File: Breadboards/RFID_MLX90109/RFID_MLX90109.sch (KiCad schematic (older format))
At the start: 0 parts

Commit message: Transfers RFID schematic from Nestbox_v2 into BB
The RFID part of the Nestbox_v2 schematic was spun out into the MLX90109
BB schematic.
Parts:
- added AE?: Antenna_Loop, symbol Antenna_Loop
- added AE? (x6): Antenna_Dipole, symbol Antenna_Dipole
- added C? (x5): C, symbol C
- added JP?: Jumper_SELECT_Dual, symbol Jumper_SELECT_Dual
- added Q?: Q_NMOS_DGS, symbol Q_NMOS_DGS
- added R?: 36k, symbol R
- added R?: 100k, symbol R
- added R? (x6): R, symbol R
- added U?: MLX90109, symbol MLX90109
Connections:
- new net: AE?.1, AE?.1, AE?.1, C?.2, C?.2, C?.2, C?.2, U?.1 (COIL)
- new net: R?.1, R?.1, U?.3 (SPEED)
- new net: C?.1, R?.1, R?.2, U?.4 (MODU)
- new net: R?.1, R?.2, U?.5 (MODE)
- new net: Q?.1 (D), R?.1
- new net: AE?.1, AE?.2 (x4)
- new net +3V3: JP?.3
- new net +5V: JP?.1
- new net GND: Q?.3 (S), R?.1, R?.2, U?.2 (VSS)
- new net RFID_CLOCK: R?.2, U?.6 (CLOCK)
- new net RFID_DATA: R?.2, U?.7 (DATA)
- new net RFID_MODU_N: Q?.2 (G)
- new net RFID_VDD: AE?.2, AE?.2, AE?.2, C?.1, C?.1, C?.1, C?.1, C?.2, JP?.2, R?.1, R?.1, R?.2, R?.2, R?.2, U?.8 (VDD)
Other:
- note added: "0.87 V"
- note added: "Pull to GND for Operation\nPull to VDD for Standby\n"

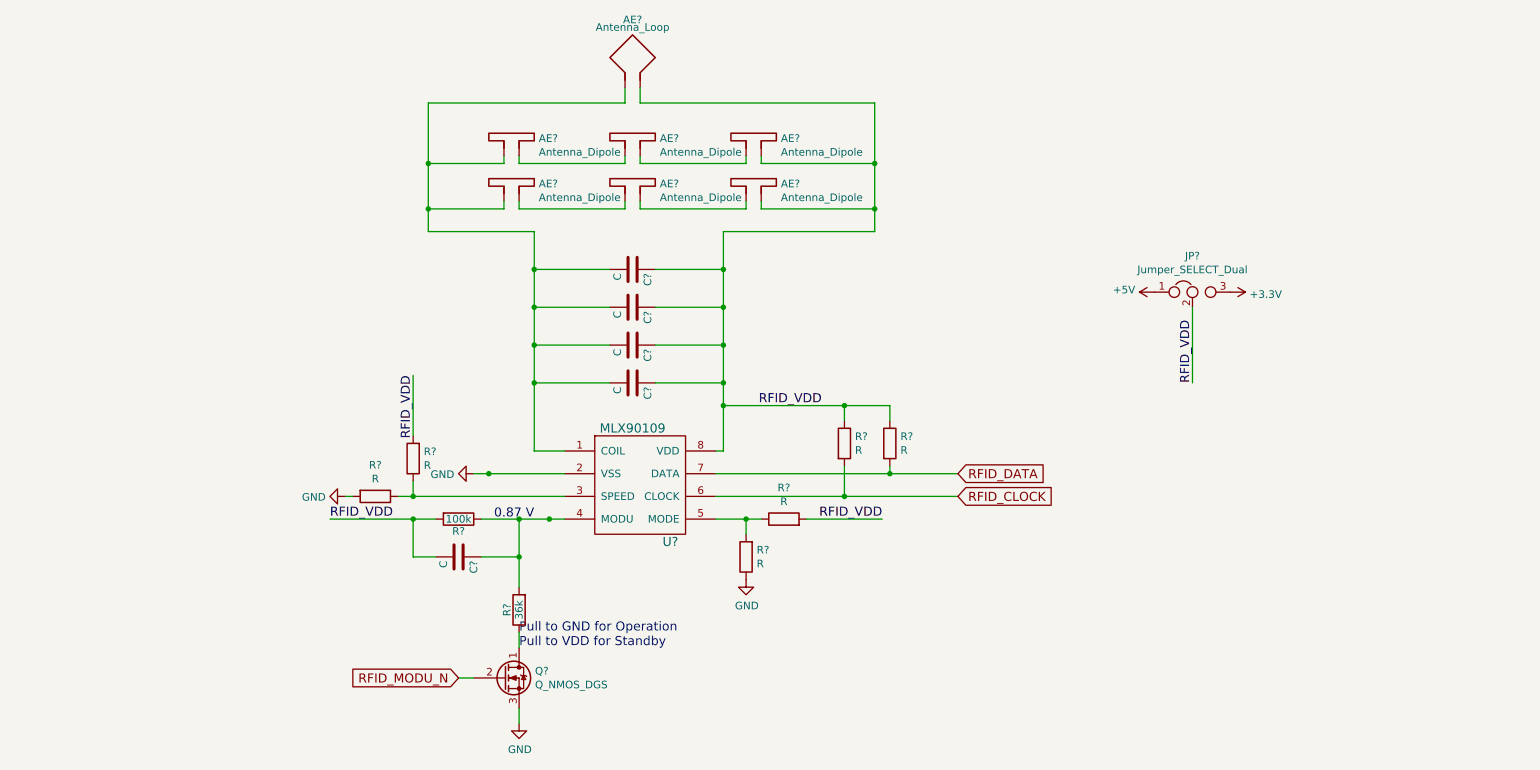
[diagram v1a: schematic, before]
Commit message: Adds connector for all signals
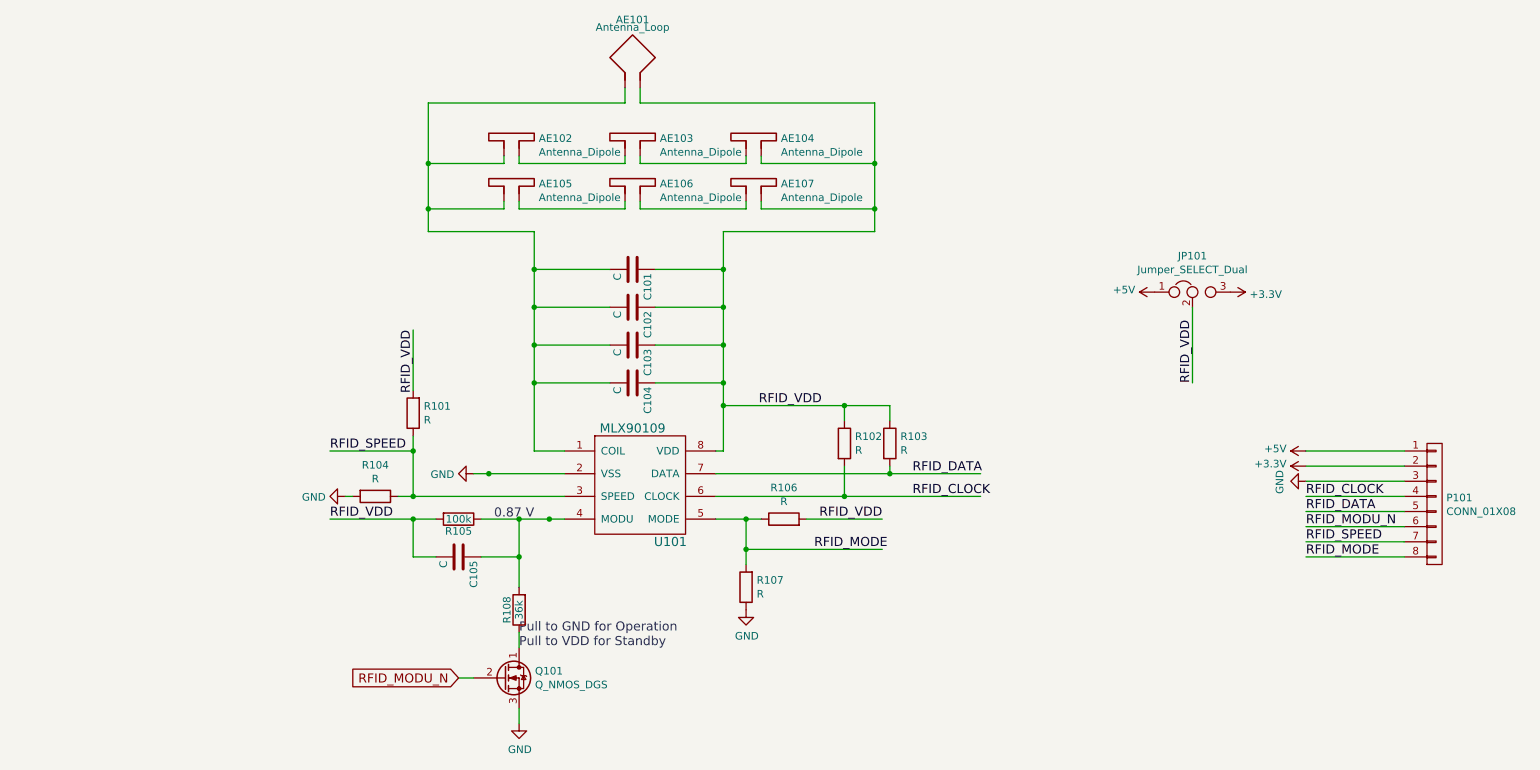
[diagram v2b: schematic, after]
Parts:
- added P101: CONN_01X08, symbol CONN_01X08
- gave numbers to parts that had none: 23
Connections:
- net labels added: RFID_MODE, RFID_SPEED
- wire segments 65 -> 75
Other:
- moved on the sheet: R101, R107

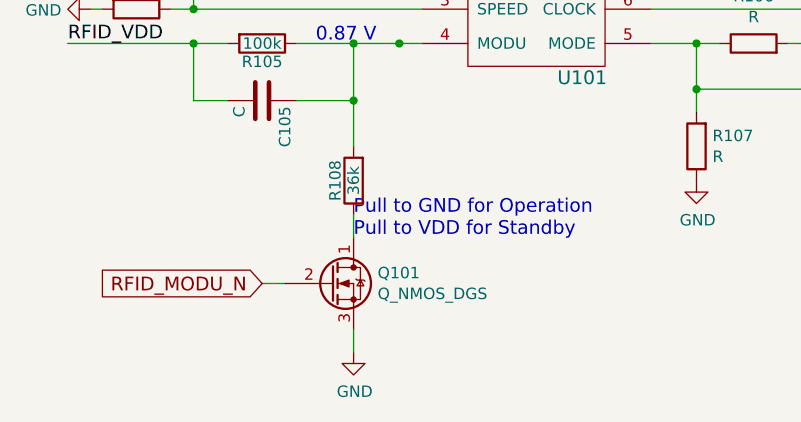
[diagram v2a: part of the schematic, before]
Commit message: Maps all components to Footprints
- All components have a now a footprint associated.
- The Pull down MOSFET was changed to GSD, to follow the SOT-23 package.
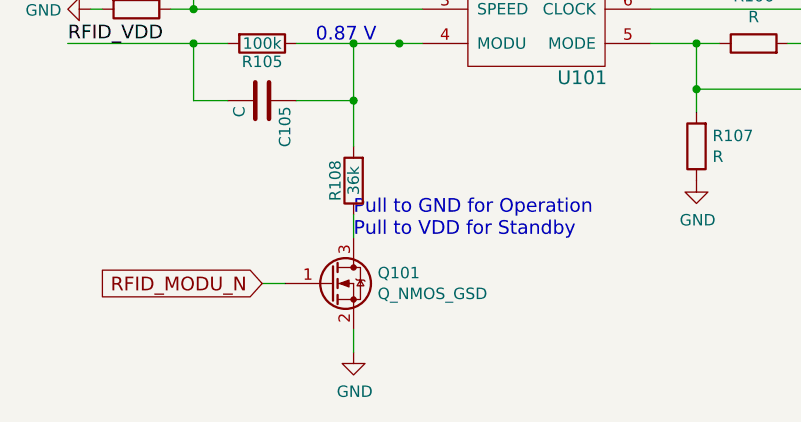
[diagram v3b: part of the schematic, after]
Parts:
- removed Q101: Q_NMOS_DGS, symbol Q_NMOS_DGS
- added Q101: Q_NMOS_GSD, TO_SOT_Packages_SMD:SOT-23_Handsoldering, symbol Q_NMOS_GSD
- AE101: footprint (none) -> Resistors_THT:R_Axial_DIN0411_L9.9mm_D3.6mm_P25.40mm_Horizontal
- AE102, AE103, AE104, AE105, AE106, AE107: footprint (none) -> Octanis3:TDK_B82450A
- C101, C102: footprint (none) -> Capacitors_THT:C_Rect_L7.0mm_W3.5mm_P5.00mm
- C103, C104, C105: footprint (none) -> Capacitors_SMD:C_0805_HandSoldering
- JP101: footprint (none) -> Pin_Headers:Pin_Header_Straight_1x03_Pitch2.54mm
- P101: footprint (none) -> Pin_Headers:Pin_Header_Straight_1x08_Pitch2.54mm
- R101, R102, R103, R104, R105, R106, R107, R108: footprint (none) -> Resistors_SMD:R_0603_HandSoldering
- U101: footprint (none) -> Housings_SOIC:SOIC-8_3.9x4.9mm_Pitch1.27mm
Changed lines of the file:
@@
 F 0 "U101" H 5500 2600 60  0000 C CNN
 F 1 "MLX90109" H 5250 3350 60  0000 C CNN
-F 2 "" H 5250 3350 60  0001 C CNN
+F 2 "Housings_SOIC:SOIC-8_3.9x4.9mm_Pitch1.27mm" H 5250 3350 60  0001 C CNN
 F 3 "" H 5250 3350 60  0001 C CNN
 	1    5250 3350
@@
 F 0 "R108" V 4580 4550 50  0000 C CNN
 F 1 "36k" V 4500 4550 50  0000 C CNN
-F 2 "" V 4430 4550 50  0001 C CNN
+F 2 "Resistors_SMD:R_0603_HandSoldering" V 4430 4550 50  0001 C CNN
 F 3 "" H 4500 4550 50  0001 C CNN
 	1    4500 4550
@@
 F 0 "R105" V 4180 3950 50  0000 C CNN
 F 1 "100k" V 4100 3950 50  0000 C CNN
-F 2 "" V 4030 3950 50  0001 C CNN
+F 2 "Resistors_SMD:R_0603_HandSoldering" V 4030 3950 50  0001 C CNN
 F 3 "" H 4100 3950 50  0001 C CNN
 	1    4100 3950
@@
 F 0 "C104" H 5275 3150 50  0000 L CNN
 F 1 "C" H 5275 2950 50  0000 L CNN
-F 2 "" H 5288 2900 50  0001 C CNN
+F 2 "Capacitors_SMD:C_0805_HandSoldering" H 5288 2900 50  0001 C CNN
 F 3 "" H 5250 3050 50  0001 C CNN
 	1    5250 3050
@@
 F 0 "AE101" H 5250 1150 50  0000 C CNN
 F 1 "Antenna_Loop" H 5250 1100 50  0000 C CNN
-F 2 "" H 5200 900 50  0001 C CNN
+F 2 "Resistors_THT:R_Axial_DIN0411_L9.9mm_D3.6mm_P25.40mm_Horizontal" H 5200 900 50  0001 C CNN
 F 3 "" H 5200 900 50  0001 C CNN
 	1    5200 900
@@
 F 0 "C105" H 4125 4300 50  0000 L CNN
 F 1 "C" H 4125 4100 50  0000 L CNN
-F 2 "" H 4138 4050 50  0001 C CNN
+F 2 "Capacitors_SMD:C_0805_HandSoldering" H 4138 4050 50  0001 C CNN
 F 3 "" H 4100 4200 50  0001 C CNN
 	1    4100 4200
@@
 F 0 "C103" H 5275 2900 50  0000 L CNN
 F 1 "C" H 5275 2700 50  0000 L CNN
-F 2 "" H 5288 2650 50  0001 C CNN
+F 2 "Capacitors_SMD:C_0805_HandSoldering" H 5288 2650 50  0001 C CNN
 F 3 "" H 5250 2800 50  0001 C CNN
 	1    5250 2800
@@
 F 0 "C102" H 5275 2650 50  0000 L CNN
 F 1 "C" H 5275 2450 50  0000 L CNN
-F 2 "" H 5288 2400 50  0001 C CNN
+F 2 "Capacitors_THT:C_Rect_L7.0mm_W3.5mm_P5.00mm" H 5288 2400 50  0001 C CNN
 F 3 "" H 5250 2550 50  0001 C CNN
 	1    5250 2550
@@
 F 0 "C101" H 5275 2400 50  0000 L CNN
 F 1 "C" H 5275 2200 50  0000 L CNN
-F 2 "" H 5288 2150 50  0001 C CNN
+F 2 "Capacitors_THT:C_Rect_L7.0mm_W3.5mm_P5.00mm" H 5288 2150 50  0001 C CNN
 F 3 "" H 5250 2300 50  0001 C CNN
 	1    5250 2300
@@
 $EndComp
 $Comp
-L +3.3V #PWR102
+L +3.3V #PWR01
 U 1 1 5A0F0963
 P 9200 2450
-F 0 "#PWR102" H 9200 2300 50  0001 C CNN
+F 0 "#PWR01" H 9200 2300 50  0001 C CNN
 F 1 "+3.3V" V 9215 2578 50  0000 L CNN
 F 2 "" H 9200 2450 50  0000 C CNN
@@
 F 0 "JP101" H 8950 2689 50  0000 C CNN
 F 1 "Jumper_SELECT_Dual" H 8950 2598 50  0000 C CNN
-F 2 "" H 8950 2450 50  0001 C CNN
+F 2 "Pin_Headers:Pin_Header_Straight_1x03_Pitch2.54mm" H 8950 2450 50  0001 C CNN
 F 3 "" H 8950 2450 50  0001 C CNN
 	1    8950 2450
@@
 RFID_VDD
 $Comp
-L +5V #PWR101
+L +5V #PWR02
 U 1 1 5A0F0965
 P 8700 2450
-F 0 "#PWR101" H 8700 2300 50  0001 C CNN
+F 0 "#PWR02" H 8700 2300 50  0001 C CNN
 F 1 "+5V" V 8715 2578 50  0000 L CNN
 F 2 "" H 8700 2450 50  0001 C CNN
@@
 $EndComp
 $Comp
-L GND #PWR105
+L GND #PWR03
 U 1 1 5A0F0966
 P 4200 3650
-F 0 "#PWR105" H 4200 3400 50  0001 C CNN
+F 0 "#PWR03" H 4200 3400 50  0001 C CNN
 F 1 "GND" V 4205 3522 50  0000 R CNN
 F 2 "" H 4200 3650 50  0001 C CNN
@@
 F 0 "R104" V 3343 3800 50  0000 C CNN
 F 1 "R" V 3434 3800 50  0000 C CNN
-F 2 "" V 3480 3800 50  0001 C CNN
+F 2 "Resistors_SMD:R_0603_HandSoldering" V 3480 3800 50  0001 C CNN
 F 3 "" H 3550 3800 50  0001 C CNN
 	1    3550 3800
@@
 F 0 "R101" H 3730 3204 50  0000 R CNN
 F 1 "R" H 3730 3295 50  0000 R CNN
-F 2 "" V 3730 3250 50  0001 C CNN
+F 2 "Resistors_SMD:R_0603_HandSoldering" V 3730 3250 50  0001 C CNN
 F 3 "" H 3800 3250 50  0001 C CNN
 	1    3800 3250
@@
 RFID_VDD
 $Comp
-L GND #PWR107
+L GND #PWR04
 U 1 1 5A0F0969
 P 3350 3800
-F 0 "#PWR107" H 3350 3550 50  0001 C CNN
+F 0 "#PWR04" H 3350 3550 50  0001 C CNN
 F 1 "GND" V 3355 3672 50  0000 R CNN
 F 2 "" H 3350 3800 50  0001 C CNN
@@
 F 0 "R107" H 5930 4354 50  0000 R CNN
 F 1 "R" H 5930 4445 50  0000 R CNN
-F 2 "" V 5930 4400 50  0001 C CNN
+F 2 "Resistors_SMD:R_0603_HandSoldering" V 5930 4400 50  0001 C CNN
 F 3 "" H 6000 4400 50  0001 C CNN
 	1    6000 4400
@@
 F 0 "R106" V 6457 3950 50  0000 C CNN
 F 1 "R" V 6366 3950 50  0000 C CNN
-F 2 "" V 6180 3950 50  0001 C CNN
+F 2 "Resistors_SMD:R_0603_HandSoldering" V 6180 3950 50  0001 C CNN
 F 3 "" H 6250 3950 50  0001 C CNN
 	1    6250 3950
@@
 $EndComp
 $Comp
-L GND #PWR108
+L GND #PWR05
 U 1 1 5A0F096C
 P 6000 4550
-F 0 "#PWR108" H 6000 4300 50  0001 C CNN
+F 0 "#PWR05" H 6000 4300 50  0001 C CNN
 F 1 "GND" H 6005 4377 50  0000 C CNN
 F 2 "" H 6000 4550 50  0001 C CNN
@@
 RFID_VDD
 $Comp
-L Q_NMOS_DGS Q101
-U 1 1 5A0F096D
-P 4400 5000
-F 0 "Q101" H 4605 5046 50  0000 L CNN
-F 1 "Q_NMOS_DGS" H 4605 4955 50  0000 L CNN
-F 2 "" H 4600 5100 50  0001 C CNN
-F 3 "" H 4400 5000 50  0001 C CNN
-	1    4400 5000
-	1    0    0    -1
-$EndComp
-$Comp
-L GND #PWR109
+L GND #PWR06
 U 1 1 5A0F096E
 P 4500 5300
-F 0 "#PWR109" H 4500 5050 50  0001 C CNN
+F 0 "#PWR06" H 4500 5050 50  0001 C CNN
 F 1 "GND" H 4505 5127 50  0000 C CNN
 F 2 "" H 4500 5300 50  0001 C CNN
@@
 F 0 "R102" H 6720 3496 50  0000 L CNN
 F 1 "R" H 6720 3405 50  0000 L CNN
-F 2 "" V 6580 3450 50  0001 C CNN
+F 2 "Resistors_SMD:R_0603_HandSoldering" V 6580 3450 50  0001 C CNN
 F 3 "" H 6650 3450 50  0001 C CNN
 	1    6650 3450
@@
 F 0 "R103" H 7020 3496 50  0000 L CNN
 F 1 "R" H 7020 3405 50  0000 L CNN
-F 2 "" V 6880 3450 50  0001 C CNN
+F 2 "Resistors_SMD:R_0603_HandSoldering" V 6880 3450 50  0001 C CNN
 F 3 "" H 6950 3450 50  0001 C CNN
 	1    6950 3450
@@
 F 0 "AE102" H 4630 1266 50  0000 L CNN
 F 1 "Antenna_Dipole" H 4630 1175 50  0000 L CNN
-F 2 "" H 4400 1350 50  0001 C CNN
+F 2 "Octanis3:TDK_B82450A" H 4400 1350 50  0001 C CNN
 F 3 "" H 4400 1350 50  0001 C CNN
 	1    4400 1350
@@
 F 0 "AE103" H 5430 1266 50  0000 L CNN
 F 1 "Antenna_Dipole" H 5430 1175 50  0000 L CNN
-F 2 "" H 5200 1350 50  0001 C CNN
+F 2 "Octanis3:TDK_B82450A" H 5200 1350 50  0001 C CNN
 F 3 "" H 5200 1350 50  0001 C CNN
 	1    5200 1350
@@
 F 0 "AE104" H 6230 1266 50  0000 L CNN
 F 1 "Antenna_Dipole" H 6230 1175 50  0000 L CNN
-F 2 "" H 6000 1350 50  0001 C CNN
+F 2 "Octanis3:TDK_B82450A" H 6000 1350 50  0001 C CNN
 F 3 "" H 6000 1350 50  0001 C CNN
 	1    6000 1350
@@
 F 0 "AE105" H 4630 1566 50  0000 L CNN
 F 1 "Antenna_Dipole" H 4630 1475 50  0000 L CNN
-F 2 "" H 4400 1650 50  0001 C CNN
+F 2 "Octanis3:TDK_B82450A" H 4400 1650 50  0001 C CNN
 F 3 "" H 4400 1650 50  0001 C CNN
 	1    4400 1650
@@
 F 0 "AE106" H 5430 1566 50  0000 L CNN
 F 1 "Antenna_Dipole" H 5430 1475 50  0000 L CNN
-F 2 "" H 5200 1650 50  0001 C CNN
+F 2 "Octanis3:TDK_B82450A" H 5200 1650 50  0001 C CNN
 F 3 "" H 5200 1650 50  0001 C CNN
 	1    5200 1650
@@
 F 0 "AE107" H 6230 1566 50  0000 L CNN
 F 1 "Antenna_Dipole" H 6230 1475 50  0000 L CNN
-F 2 "" H 6000 1650 50  0001 C CNN
+F 2 "Octanis3:TDK_B82450A" H 6000 1650 50  0001 C CNN
 F 3 "" H 6000 1650 50  0001 C CNN
 	1    6000 1650
@@
 RFID_MODU_N
 $Comp
-L +5V #PWR103
+L +5V #PWR07
 U 1 1 5A12CC37
 P 9700 3500
-F 0 "#PWR103" H 9700 3350 50  0001 C CNN
+F 0 "#PWR07" H 9700 3350 50  0001 C CNN
 F 1 "+5V" V 9715 3628 50  0000 L CNN
 F 2 "" H 9700 3500 50  0001 C CNN
@@
 $EndComp
 $Comp
-L +3.3V #PWR104
+L +3.3V #PWR08
 U 1 1 5A12CC72
 P 9700 3600
-F 0 "#PWR104" H 9700 3450 50  0001 C CNN
+F 0 "#PWR08" H 9700 3450 50  0001 C CNN
 F 1 "+3.3V" V 9715 3728 50  0000 L CNN
 F 2 "" H 9700 3600 50  0000 C CNN
@@
 $EndComp
 $Comp
-L GND #PWR106
+L GND #PWR09
 U 1 1 5A12CCDD
 P 9700 3700
-F 0 "#PWR106" H 9700 3450 50  0001 C CNN
+F 0 "#PWR09" H 9700 3450 50  0001 C CNN
 F 1 "GND" H 9705 3527 50  0000 C CNN
 F 2 "" H 9700 3700 50  0001 C CNN
@@
 F 0 "P101" H 10628 3891 50  0000 L CNN
 F 1 "CONN_01X08" H 10628 3800 50  0000 L CNN
-F 2 "" H 10550 3850 50  0000 C CNN
+F 2 "Pin_Headers:Pin_Header_Straight_1x08_Pitch2.54mm" H 10550 3850 50  0001 C CNN
 F 3 "" H 10550 3850 50  0000 C CNN
 	1    10550 3850
@@
 Text Label 9700 4200 0    60   ~ 0
 RFID_MODE
+$Comp
+L Q_NMOS_GSD Q101
+U 1 1 5A12C975
+P 4400 5000
+F 0 "Q101" H 4605 5046 50  0000 L CNN
+F 1 "Q_NMOS_GSD" H 4605 4955 50  0000 L CNN
+F 2 "TO_SOT_Packages_SMD:SOT-23_Handsoldering" H 4600 5100 50  0001 C CNN
+F 3 "" H 4400 5000 50  0000 C CNN
+F 4 "726-BSS127H6327" H 4400 5000 60  0001 C CNN "Mouser-Part"
+	1    4400 5000
+	1    0    0    -1
+$EndComp
 $EndSCHEMATC
